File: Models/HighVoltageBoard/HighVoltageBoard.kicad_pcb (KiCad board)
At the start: 2 copper layers, 0 parts

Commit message: Save progress
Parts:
- added REF**: MountingHole_2.2mm_M2_DIN965_Pad, MountingHole:MountingHole_2.2mm_M2_DIN965_Pad, F.Cu at (152.9, 114.2)
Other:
- board text removed: "Layer 4: signals and power Layer 3: GND (temp.) Layer 2: signals and power (temp.) Layer 1: GND violates IPC-2221 clearance of 0.25 mm only permit 0.2 mm distance to GND never allow between two high voltage conductors, which could be 900V instead of 450V minimize length of regions with 0.2 mm distance to GND conductor high voltage vias should respect 0.8 mm clearance to GND conductor DESIGN REVIS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"
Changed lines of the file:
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@@
 	)
 	(net 0 "")
-	(gr_text "Layer 4: signals and power\nLayer 3: GND (temp.)\nLayer 2: signals and power (temp.)\nLayer 1: GND\n\nviolates IPC-2221 clearance of 0.25 mm\nonly permit 0.2 mm distance to GND\nnever allow between two high voltage conductors,\nwhich could be 900V instead of 450V\n\nminimize length of regions with\n0.2 mm distance to GND conductor\n\nhigh voltage vias should respect 0.8 mm\nclearance to GND conductor\n\nDESIGN REVISION: 4-layer PCB\nno longer needed or helpful\nfor the routing problem"
-		(at 134.9 166.9 0)
-		(layer "Cmts.User")
-		(effects
-			(font
-				(size 0.8 0.8)
-				(thickness 0.12)
+	(footprint "MountingHole:MountingHole_2.2mm_M2_DIN965_Pad"
+		(layer "F.Cu")
+		(at 152.86 114.15)
+		(descr "Mounting Hole 2.2mm, M2, generated by kicad-footprint-generator mountinghole.py")
+		(tags "mountinghole M2 DIN965")
+		(property "Reference" "REF**"
+			(at 0 -2.85 0)
+			(layer "F.SilkS")
+			(effects
+				(font
+					(size 1 1)
+					(thickness 0.15)
+				)
 			)
-			(justify left top)
 		)
+		(property "Value" "MountingHole_2.2mm_M2_DIN965_Pad"
+			(at 0 2.85 0)
+			(layer "F.Fab")
+			(effects
+				(font
+					(size 1 1)
+					(thickness 0.15)
+				)
+			)
+		)
+		(property "Datasheet" ""
+			(at 0 0 0)
+			(layer "F.Fab")
+			(hide yes)
+			(effects
+				(font
+					(size 1.27 1.27)
+					(thickness 0.15)
+				)
+			)
+		)
+		(property "Description" ""
+			(at 0 0 0)
+			(layer "F.Fab")
+			(hide yes)
+			(effects
+				(font
+					(size 1.27 1.27)
+					(thickness 0.15)
+				)
+			)
+		)
+		(attr exclude_from_pos_files exclude_from_bom)
+		(fp_circle
+			(center 0 0)
+			(end 1.9 0)
+			(stroke
+				(width 0.15)
+				(type solid)
+			)
+			(fill no)
+			(layer "Cmts.User")
+		)
+		(fp_circle
+			(center 0 0)
+			(end 2.15 0)
+			(stroke
+				(width 0.05)
+				(type solid)
+			)
+			(fill no)
+			(layer "F.CrtYd")
+		)
+		(fp_text user "${REFERENCE}"
+			(at 0 0 0)
+			(layer "F.Fab")
+			(effects
+				(font
+					(size 0.95 0.95)
+					(thickness 0.14)
+				)
+			)
+		)
+		(pad "1" thru_hole circle
+			(at 0 0)
+			(size 3.8 3.8)
+			(drill 2.2)
+			(layers "*.Cu" "*.Mask")
+			(remove_unused_layers no)
+			(zone_connect 2)
+		)
+		(embedded_fonts no)
 	)
 	(embedded_fonts no)

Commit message: Finished THT footprints
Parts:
- removed the REF** at (152.9, 114.2)
- added REF**: RFPC-SMA27-F, Connector_Custom:RFPC-SMA27-F, F.Cu at (145.9, 123.3)
- added REF**: Multicomp_24.243, Connector_Custom:Multicomp_24.243, F.Cu at (154.6, 101.4)
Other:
- board outline added: 50.5 x 37.2 mm

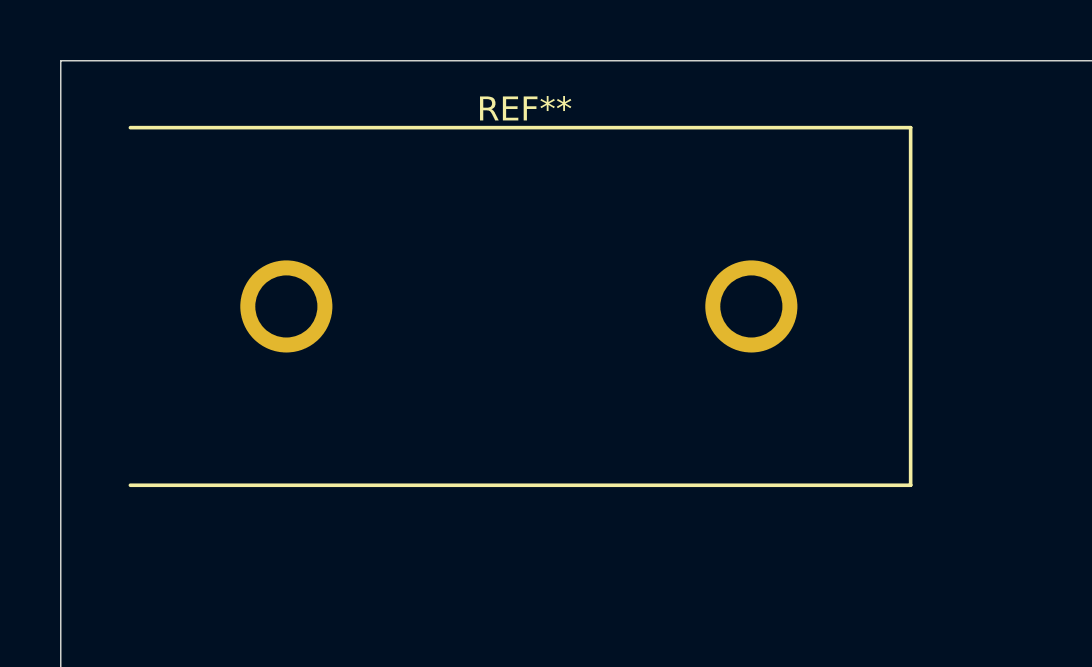
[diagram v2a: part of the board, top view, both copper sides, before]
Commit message: Finished designing the footprints
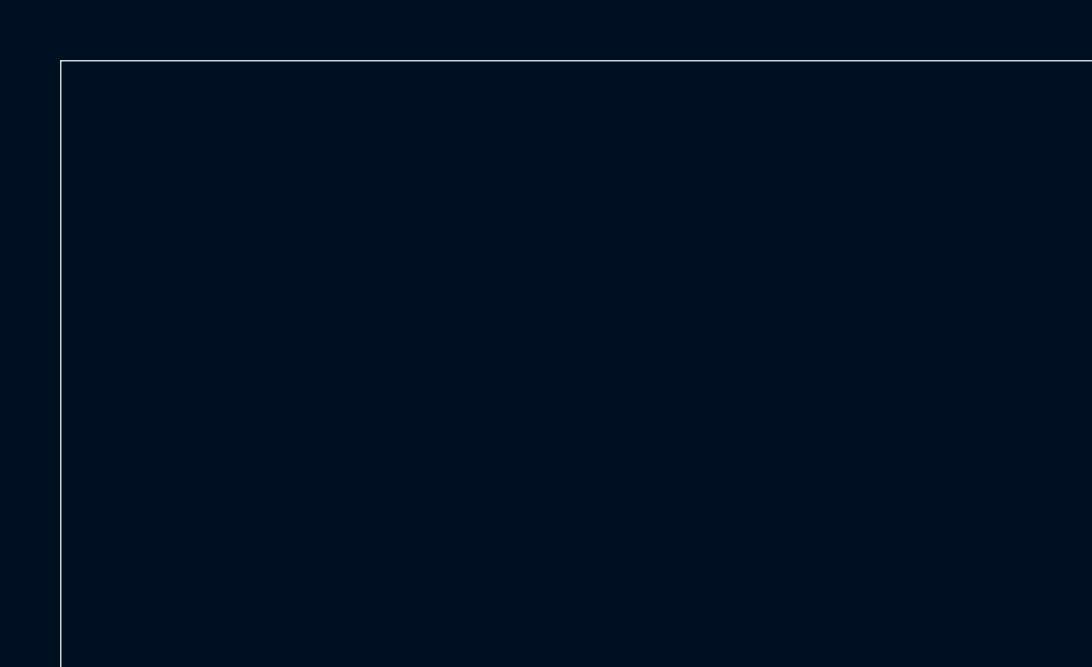
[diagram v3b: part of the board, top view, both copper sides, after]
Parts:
- removed the REF** at (154.6, 101.4)
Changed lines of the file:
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@@
-		(embedded_fonts no)
-	)
-	(footprint "Connector_Custom:Multicomp_24.243"
-		(layer "F.Cu")
-		(at 154.57 101.38)
-		(property "Reference" "REF**"
-			(at 0.19 -6.57 0)
-			(unlocked yes)
-			(layer "F.SilkS")
-			(effects
-				(font
-					(size 0.8 0.8)
-					(thickness 0.12)
-				)
-			)
-		)
-		(property "Value" "Multicomp_24.243"
-			(at 0.19 -5.37 0)
-			(unlocked yes)
-			(layer "F.Fab")
-			(effects
-				(font
-					(size 0.8 0.8)
-					(thickness 0.12)
-				)
-			)
-		)
-		(property "Datasheet" ""
-			(at 0 0 0)
-			(unlocked yes)
-			(layer "F.Fab")
-			(hide yes)
-			(effects
-				(font
-					(size 0.8 0.8)
-					(thickness 0.12)
-				)
-			)
-		)
-		(property "Description" ""
-			(at 0 0 0)
-			(unlocked yes)
-			(layer "F.Fab")
-			(hide yes)
-			(effects
-				(font
-					(size 0.8 0.8)
-					(thickness 0.12)
-				)
-			)
-		)
-		(attr through_hole)
-		(fp_line
-			(start 13.06 -5.96)
-			(end -12.95 -5.96)
-			(stroke
-				(width 0.12)
-				(type default)
-			)
-			(layer "F.SilkS")
-		)
-		(fp_line
-			(start 13.06 -5.96)
-			(end 13.06 5.96)
-			(stroke
-				(width 0.12)
-				(type default)
-			)
-			(layer "F.SilkS")
-		)
-		(fp_line
-			(start 13.06 5.96)
-			(end -12.95 5.96)
-			(stroke
-				(width 0.12)
-				(type default)
-			)
-			(layer "F.SilkS")
-		)
-		(fp_rect
-			(start -13.45 -6.35)
-			(end 13.45 6.35)
-			(stroke
-				(width 0.05)
-				(type default)
-			)
-			(fill no)
-			(layer "F.CrtYd")
-		)
-		(fp_rect
-			(start -12.95 -5.85)
-			(end 12.95 5.85)
-			(stroke
-				(width 0.1)
-				(type default)
-			)
-			(fill no)
-			(layer "F.Fab")
-		)
-		(fp_text user "${REFERENCE}"
-			(at 0.19 -4.17 0)
-			(unlocked yes)
-			(layer "F.Fab")
-			(effects
-				(font
-					(size 0.8 0.8)
-					(thickness 0.12)
-				)
-			)
-		)
-		(pad "1" thru_hole circle
-			(at -7.75 0)
-			(size 3.07 3.07)
-			(drill 2.07)
-			(layers "*.Cu" "*.Mask")
-			(remove_unused_layers no)
-		)
-		(pad "2" thru_hole circle
-			(at 7.75 0)
-			(size 3.07 3.07)
-			(drill 2.07)
-			(layers "*.Cu" "*.Mask")
-			(remove_unused_layers no)
-		)
 		(embedded_fonts no)
 	)

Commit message: Starting layout of the high voltage board
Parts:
- removed REF**: RFPC-SMA27-F, Connector_Custom:RFPC-SMA27-F
- added C1: 47 nF, 630V, TwoTerminal:CAPC2220_GRJ, F.Cu at (83.8, 134.5)
- added C10: 47 nF, 630V, TwoTerminal:CAPC2220_GRJ, F.Cu at (100.7, 33.0)
- added C11: 47 nF, 630V, TwoTerminal:CAPC2220_GRJ, F.Cu at (100.7, 25.5)
- added C12: 10 pF, 1 kV, TwoTerminal:CAPC1206_CHV, F.Cu at (114.0, 25.8)
- added C2: 47 nF, 630V, TwoTerminal:CAPC2220_GRJ, F.Cu at (92.1, 130.4)
- added C3: 10 pF, 1 kV, TwoTerminal:CAPC1206_CHV, F.Cu at (107.6, 132.4)
- added C4: 47 nF, 630V, TwoTerminal:CAPC2220_GRJ, F.Cu at (99.0, 97.8)
- added C5: 47 nF, 630V, TwoTerminal:CAPC2220_GRJ, F.Cu at (99.0, 90.3)
- added C6: 10 pF, 1 kV, TwoTerminal:CAPC1206_CHV, F.Cu at (112.4, 90.6)
- added C7: 47 nF, 630V, TwoTerminal:CAPC2220_GRJ, F.Cu at (100.4, 65.3)
- added C8: 47 nF, 630V, TwoTerminal:CAPC2220_GRJ, F.Cu at (100.4, 57.8)
- added C9: 10 pF, 1 kV, TwoTerminal:CAPC1206_CHV, F.Cu at (113.7, 58.1)
- added D1: Vr = 2 kV, TwoTerminal:DO-214AC, F.Cu at (214.4, 77.8)
- added D2: Vr = 2 kV, TwoTerminal:DO-214AC, F.Cu at (214.4, 52.7)
- added D3: Vr = 451V, TwoTerminal:DO-214AA, F.Cu at (214.4, 69.1)
- added D4: Vr = 451V, TwoTerminal:DO-214AA, F.Cu at (214.3, 61.2)
- added H1: Mounting Hole, M2.5, Connector_Custom:Keystone_24929, F.Cu at (232.4, 106.3)
- added H2: Mounting Hole, M2.5, Connector_Custom:Keystone_24929, F.Cu at (232.4, 114.1)
- added H3: Dowel Pin, M2.5, Connector_Custom:DowelPin_2.5mm, F.Cu at (238.1, 104.3)
- added H4: Mounting Hole, M2.5, Connector_Custom:Keystone_24929, F.Cu at (232.4, 121.8)
- added H5: Mounting Hole, M2.5, Connector_Custom:Keystone_24929, F.Cu at (232.4, 129.6)
- added H6: Dowel Pin, M2.5, Connector_Custom:DowelPin_2.5mm, F.Cu at (238.1, 107.9)
- added J1: Conn_01x13_Socket, Connector_Custom:PinConnector_1x13, F.Cu at (231.0, 149.4)
- added J10: Conn_01x04_Socket, Connector_Custom:PinConnector_1x4, F.Cu at (93.7, 62.7)
- added J11: Conn_Coaxial, Connector_Custom:RFPC-SMA27-F, F.Cu at (109.7, 32.1)
- added J12: Conn_01x04_Socket, Connector_Custom:PinConnector_1x4, F.Cu at (94.0, 30.4)
- added J2: Banana Socket, Red, Connector_Custom:Multicomp_24.243, F.Cu at (231.1, 78.6)
- added J3: Banana Socket, Black, Connector_Custom:Multicomp_24.243, F.Cu at (231.1, 64.9)
- added J4: Banana Socket, Yellow, Connector_Custom:Multicomp_24.243, F.Cu at (231.1, 51.1)
- added J5: Conn_Coaxial, Connector_Custom:RFPC-SMA27-F, F.Cu at (61.4, 129.6)
- added J6: Conn_01x04_Socket, Connector_Custom:PinConnector_1x4, F.Cu at (63.1, 135.6)
- added J7: Conn_Coaxial, Connector_Custom:RFPC-SMA27-F, F.Cu at (108.0, 97.0)
- added J8: Conn_01x04_Socket, Connector_Custom:PinConnector_1x4, F.Cu at (92.4, 95.3)
- added J9: Conn_Coaxial, Connector_Custom:RFPC-SMA27-F, F.Cu at (109.3, 64.4)
- added NT1: NetTie_2, Connector_Custom:NetTie_0.2mm, F.Cu at (102.5, 130.8)
- added NT2: NetTie_2, Connector_Custom:NetTie_0.2mm, F.Cu at (120.2, 127.7)
- added NT3: NetTie_2, Connector_Custom:NetTie_0.2mm, F.Cu at (108.5, 91.6)
- added NT4: NetTie_2, Connector_Custom:NetTie_0.2mm, F.Cu at (108.5, 90.1)
- added NT5: NetTie_2, Connector_Custom:NetTie_0.2mm, F.Cu at (109.8, 59.1)
- added NT6: NetTie_2, Connector_Custom:NetTie_0.2mm, F.Cu at (109.8, 57.6)
- added NT7: NetTie_2, Connector_Custom:NetTie_0.2mm, F.Cu at (110.1, 26.8)
- added NT8: NetTie_2, Connector_Custom:NetTie_0.2mm, F.Cu at (110.1, 25.3)
- added Q1: Q_NJFET_DSG, ThreeTerminal:SOT-23, F.Cu at (118.8, 131.0)
- added Q2: Q_NJFET_DSG, ThreeTerminal:SOT-23, F.Cu at (114.8, 131.4)
- added Q3: Q_NJFET_DSG, ThreeTerminal:SOT-23, F.Cu at (118.1, 89.9)
- added Q4: Q_NJFET_DSG, ThreeTerminal:SOT-23, F.Cu at (118.1, 85.2)
- added Q5: Q_NJFET_DSG, ThreeTerminal:SOT-23, F.Cu at (119.4, 57.4)
- added Q6: Q_NJFET_DSG, ThreeTerminal:SOT-23, F.Cu at (119.4, 52.7)
- added Q7: Q_NJFET_DSG, ThreeTerminal:SOT-23, F.Cu at (119.8, 25.1)
- added Q8: Q_NJFET_DSG, ThreeTerminal:SOT-23, F.Cu at (119.8, 20.4)
- added R1: 1M, 5%, 0.33W, 800V, TwoTerminal:RESC1206_RCV, F.Cu at (209.1, 69.2)
- added R10: 1M, 0.1%, 0.33W, 1 kV, TwoTerminal:RESC1210_TNPV, F.Cu at (113.8, 54.2)
- added R11: 15, 1%, 0.25W, 1.9V, TwoTerminal:RESC0805, F.Cu at (108.3, 54.8)
- added R12: 28k, 0.1%, TwoTerminal:RESC0603, F.Cu at (108.9, 19.6)
- added R13: 1M, 0.1%, 0.33W, 1 kV, TwoTerminal:RESC1210_TNPV, F.Cu at (114.1, 21.9)
- added R14: 15, 1%, 0.25W, 1.9V, TwoTerminal:RESC0805, F.Cu at (108.6, 22.5)
- added R2: 1M, 5%, 0.33W, 800V, TwoTerminal:RESC1206_RCV, F.Cu at (209.1, 61.3)
- added R3: 28k, 0.1%, TwoTerminal:RESC0603, F.Cu at (114.8, 126.5)
- added R4: 1M, 0.1%, 0.33W, 1 kV, TwoTerminal:RESC1210_TNPV, F.Cu at (103.5, 126.7)
- added R5: 15, 1%, 0.25W, 1.9V, TwoTerminal:RESC0805, F.Cu at (101.4, 132.6)
- added R6: 28k, 0.1%, TwoTerminal:RESC0603, F.Cu at (107.2, 84.4)
- added R7: 1M, 0.1%, 0.33W, 1 kV, TwoTerminal:RESC1210_TNPV, F.Cu at (112.4, 86.7)
- added R8: 15, 1%, 0.25W, 1.9V, TwoTerminal:RESC0805, F.Cu at (107.0, 87.3)
- added R9: 28k, 0.1%, TwoTerminal:RESC0603, F.Cu at (108.6, 51.9)
- added U1: PA95, IC:PA95, F.Cu at (103.7, 137.1)
- added U2: PA95, IC:PA95, F.Cu at (103.8, 105.4)
- added U3: PA95, IC:PA95, F.Cu at (105.1, 72.9)
- added U4: PA95, IC:PA95, F.Cu at (105.4, 40.6)
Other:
- board outline removed

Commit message: Save progress
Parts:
- J10, J12, J6, J8: value Conn_01x04_Socket -> Conn_01x03_Socket; footprint Connector_Custom:PinConnector_1x4 -> Connector_Custom:PinConnector_1x3
- moved U2 12.7 mm to (103.7, 118.1)
- moved R4 7.22 mm to (110.6, 125.6)
- moved J6 5.26 mm to (60.1, 140.0)
- moved J5 4.50 mm to (60.1, 133.9)
- moved Q2 3.93 mm to (115.8, 127.6), turned to 180 degrees
- moved R3 3.40 mm to (117.8, 124.8)
- moved Q1 2.68 mm to (116.2, 131.7), turned to 0 degrees
- moved C1 1.21 mm to (83.7, 135.7)
- turned C2 to 0 degrees

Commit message: Push uncommitted changes
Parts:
- J10, J12, J6, J8: value Conn_01x03_Socket -> Conn_01x03_Pin
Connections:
- J10 pad 1: GND -> /OUTC
- J10 pad 3: /OUTC -> GND
- J12 pad 1: GND -> /OUTD
- J12 pad 3: /OUTD -> GND
- J6 pad 1: GND -> /OUTA
- J6 pad 3: /OUTA -> GND
- J8 pad 1: GND -> /OUTB
- J8 pad 3: /OUTB -> GND
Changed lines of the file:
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@@
 			)
 		)
-		(property "Value" "Conn_01x03_Socket"
+		(property "Value" "Conn_01x03_Pin"
 			(at 0.0075 -3.68 180)
 			(unlocked yes)
@@
 			(layers "*.Cu" "*.Mask")
 			(remove_unused_layers no)
-			(net 1 "GND")
+			(net 24 "/OUTC")
 			(pinfunction "Pin_1")
 			(pintype "passive")
@@
 			(layers "*.Cu" "*.Mask")
 			(remove_unused_layers no)
-			(net 24 "/OUTC")
+			(net 1 "GND")
 			(pinfunction "Pin_3")
 			(pintype "passive")
@@
 			)
 		)
-		(property "Value" "Conn_01x03_Socket"
+		(property "Value" "Conn_01x03_Pin"
 			(at 0.0075 -3.68 90)
 			(unlocked yes)
@@
 			(layers "*.Cu" "*.Mask")
 			(remove_unused_layers no)
-			(net 1 "GND")
+			(net 22 "/OUTA")
 			(pinfunction "Pin_1")
 			(pintype "passive")
@@
 			(layers "*.Cu" "*.Mask")
 			(remove_unused_layers no)
-			(net 22 "/OUTA")
+			(net 1 "GND")
 			(pinfunction "Pin_3")
 			(pintype "passive")
@@
 			)
 		)
-		(property "Value" "Conn_01x03_Socket"
+		(property "Value" "Conn_01x03_Pin"
 			(at 0.0075 -3.68 180)
 			(unlocked yes)
@@
 			(layers "*.Cu" "*.Mask")
 			(remove_unused_layers no)
-			(net 1 "GND")
+			(net 25 "/OUTD")
 			(pinfunction "Pin_1")
 			(pintype "passive")
@@
 			(layers "*.Cu" "*.Mask")
 			(remove_unused_layers no)
-			(net 25 "/OUTD")
+			(net 1 "GND")
 			(pinfunction "Pin_3")
 			(pintype "passive")
@@
 			)
 		)
-		(property "Value" "Conn_01x03_Socket"
+		(property "Value" "Conn_01x03_Pin"
 			(at 0.0075 -3.68 180)
 			(unlocked yes)
@@
 			(layers "*.Cu" "*.Mask")
 			(remove_unused_layers no)
-			(net 1 "GND")
+			(net 23 "/OUTB")
 			(pinfunction "Pin_1")
 			(pintype "passive")
@@
 			(layers "*.Cu" "*.Mask")
 			(remove_unused_layers no)
-			(net 23 "/OUTB")
+			(net 1 "GND")
 			(pinfunction "Pin_3")
 			(pintype "passive")

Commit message: Save progress
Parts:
- removed J11: Conn_Coaxial, Connector_Custom:RFPC-SMA27-F
- removed J8: Conn_01x03_Pin, Connector_Custom:PinConnector_1x3
- added J13: Conn_01x03_Pin, Connector_Custom:PinConnector_1x3, F.Cu at (92.8, 63.6)
- added J15: Conn_Coaxial, Connector_Custom:RFPC-SMA27-F, F.Cu at (109.7, 32.2)
- added J16: Conn_01x03_Pin, Connector_Custom:PinConnector_1x3, F.Cu at (93.5, 30.9)
- J12, J6: value Conn_01x03_Pin -> Conn_Coaxial; footprint Connector_Custom:PinConnector_1x3 -> Connector_Custom:RFPC-SMA27-F
- J2: value Banana Socket, Red -> Conn_01x02_Pin; footprint Connector_Custom:Multicomp_24.243 -> Connector_Custom:PinConnector_1x2
- J3: value Banana Socket, Black -> Banana Socket, Red
- J4: value Banana Socket, Yellow -> Banana Socket, Black
- J5: value Conn_Coaxial -> Banana Socket, Yellow; footprint Connector_Custom:RFPC-SMA27-F -> Connector_Custom:Multicomp_24.243
- J7: value Conn_Coaxial -> Conn_01x03_Pin; footprint Connector_Custom:RFPC-SMA27-F -> Connector_Custom:PinConnector_1x3
- moved J5 189.6 mm to (231.2, 52.0), turned to 180 degrees
- moved J7 58.2 mm to (68.5, 139.7)
- moved J2 43.4 mm to (240.8, 121.0)
- moved J12 37.5 mm to (109.4, 64.6)
- moved J9 33.1 mm to (109.1, 97.5)
- moved J10 32.2 mm to (92.2, 94.9)
- moved J3 14.3 mm to (231.2, 79.2)
- moved J4 14.3 mm to (231.2, 65.4)
- moved U2 11.9 mm to (105.0, 106.3)
- turned J6 to 0 degrees
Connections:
- J10 pad 1: /OUTC -> /OUTB
- J10 pad 2: /OUTC -> /OUTB
- J12 pad 1: /OUTD -> /OUTC
- J12 pad 2: /OUTD -> GND
- J2 pad 1: /WallPower/450V_PreDiode -> GND
- J2 pad 2: /WallPower/450V_PreDiode -> GND
- J3 pad 1: GND -> /WallPower/450V_PreDiode
- J3 pad 2: GND -> /WallPower/450V_PreDiode
- J4 pad 1: /WallPower/-450V_PreDiode -> GND
- J4 pad 2: /WallPower/-450V_PreDiode -> GND
- J5 pad 1: /OUTA -> /WallPower/-450V_PreDiode
- J5 pad 2: GND -> /WallPower/-450V_PreDiode
- J6 pad 2: /OUTA -> GND
- J7 pad 1: /OUTB -> /OUTA
- J7 pad 2: GND -> /OUTA
- J9 pad 1: /OUTC -> /OUTB

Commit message: Save progress
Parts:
- J1: footprint Connector_Custom:PinConnector_1x13 -> Connector_Custom:PinSocket_1x13
- J10, J13, J16, J7: footprint Connector_Custom:PinConnector_1x3 -> Connector_Custom:PinHeader_1x3
- J2: footprint Connector_Custom:PinConnector_1x2 -> Connector_Custom:PinHeader_1x2
